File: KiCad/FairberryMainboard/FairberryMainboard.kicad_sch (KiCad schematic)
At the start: 19 parts, among them J1 USB_Header, J2 Conn_02x03_Odd_Even, J3 Conn_02x02_Odd_Even, J4 Conn_01x02, U1 ATmega32U4-MU, U2 BBQ10KBD, Y1 Crystal_GND24

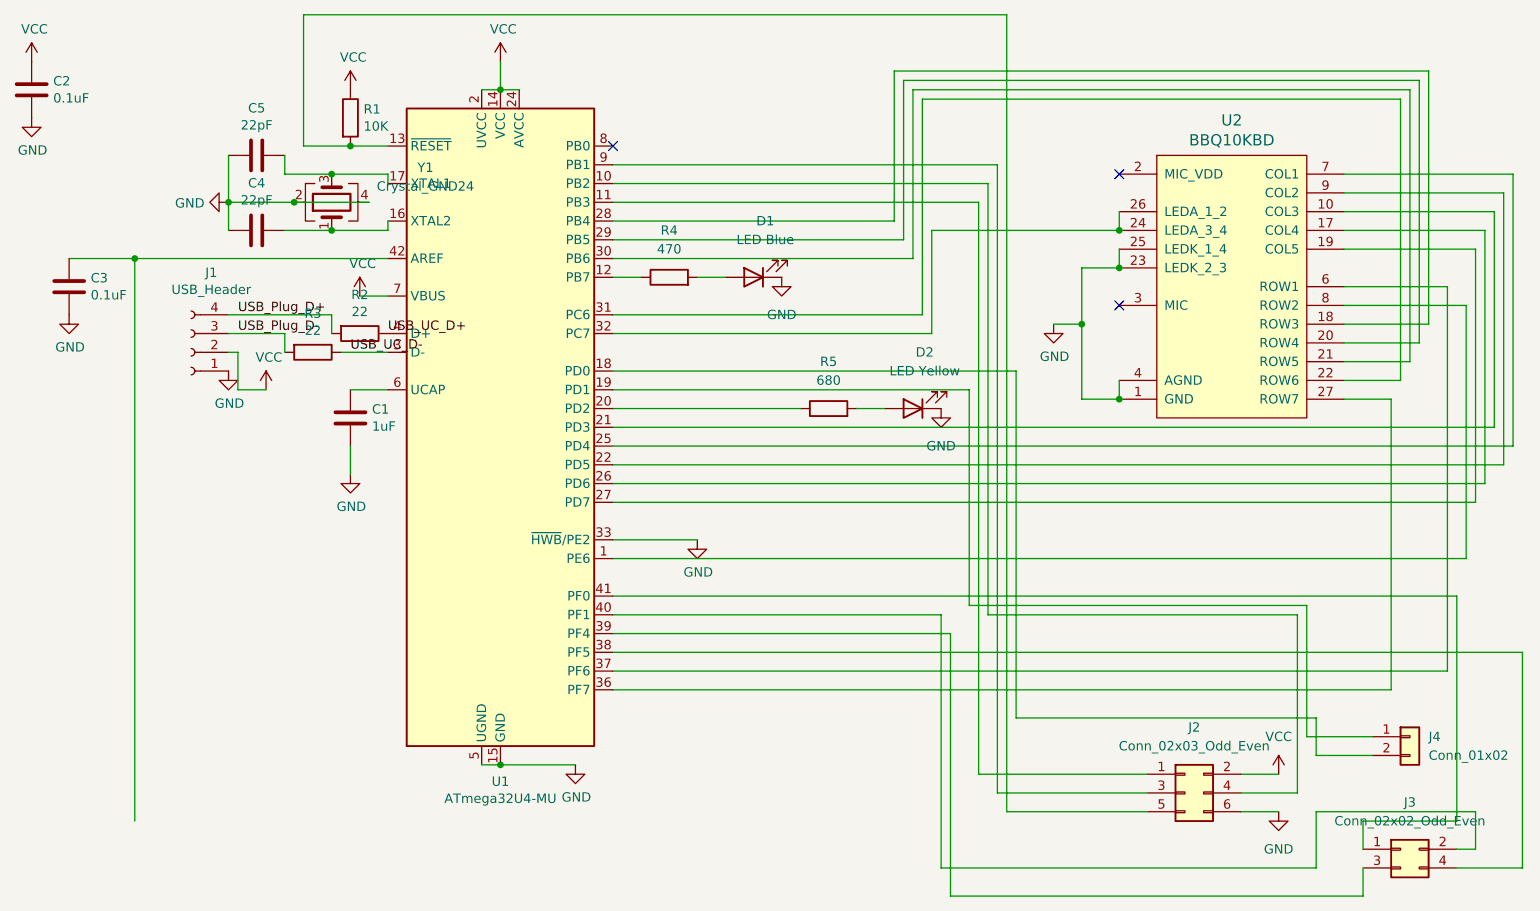
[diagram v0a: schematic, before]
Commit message: Split backlight into two zones, removed status LEDs, reduced y size by 1mm
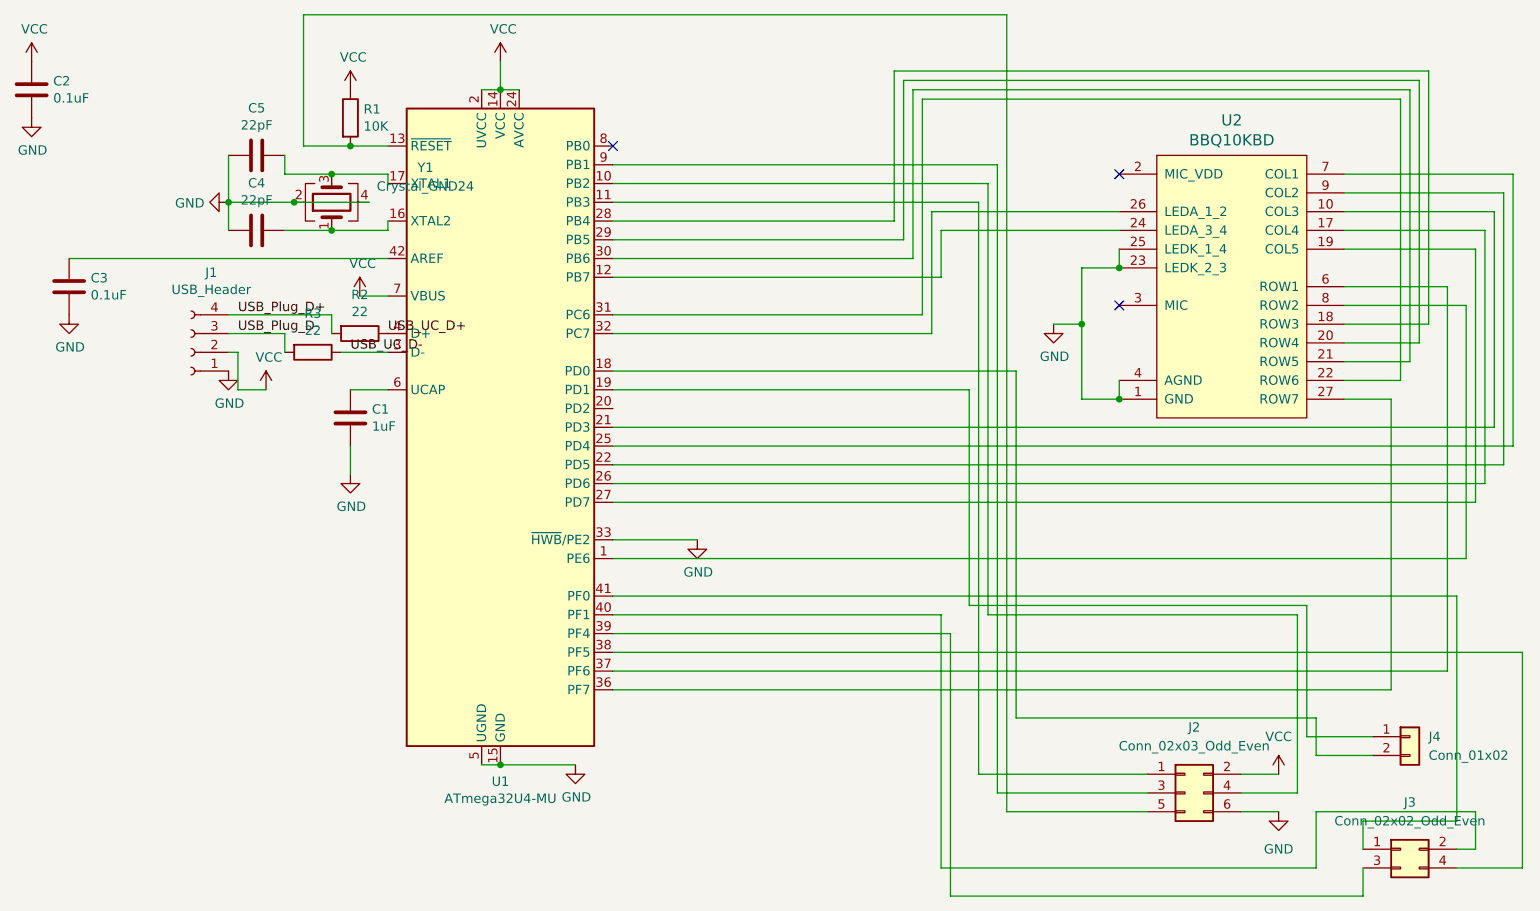
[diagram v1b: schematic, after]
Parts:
- removed D1: LED Blue, LED_SMD:LED_0603_1608Metric, symbol Device:LED
- removed D2: LED Yellow, LED_SMD:LED_0603_1608Metric, symbol Device:LED
- removed R4: 470, Resistor_SMD:R_0402_1005Metric, symbol Device:R
- removed R5: 680, Resistor_SMD:R_0402_1005Metric, symbol Device:R
- J4: footprint Fairberry:TestPoint_Pad_1x2_2.0x3.0mm -> Fairberry:TestPoint_Pad_1x2_2.0x3.0mm_Rotated
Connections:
- net at U1.12 (PB7): now also U2.24 (LEDA_3_4)
- net at U1.32 (PC7), U2.26 (LEDA_1_2): no longer U2.24 (LEDA_3_4)
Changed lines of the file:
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@@
   (junction (at 137.16 140.97) (diameter 0) (color 0 0 0 0)
   )
-  (junction (at 87.63 72.39) (diameter 0) (color 0 0 0 0)
-  )
   (junction (at 109.22 64.77) (diameter 0) (color 0 0 0 0)
   )
   (junction (at 100.33 64.77) (diameter 0) (color 0 0 0 0)
-  )
-  (junction (at 220.98 68.58) (diameter 0) (color 0 0 0 0)
   )
   (junction (at 116.84 57.15) (diameter 0) (color 0 0 0 0)
@@
     (stroke (width 0) (type default) (color 0 0 0 0))
   )
-  (wire (pts (xy 152.4 74.93) (xy 156.21 74.93))
-    (stroke (width 0) (type default) (color 0 0 0 0))
-  )
   (wire (pts (xy 212.09 81.28) (xy 215.9 81.28))
     (stroke (width 0) (type default) (color 0 0 0 0))
   )
-  (wire (pts (xy 195.58 82.55) (xy 195.58 68.58))
+  (wire (pts (xy 195.58 66.04) (xy 195.58 82.55))
     (stroke (width 0) (type default) (color 0 0 0 0))
   )
@@
     (stroke (width 0) (type default) (color 0 0 0 0))
   )
-  (wire (pts (xy 78.74 72.39) (xy 87.63 72.39))
-    (stroke (width 0) (type default) (color 0 0 0 0))
-  )
   (wire (pts (xy 251.46 60.96) (xy 274.32 60.96))
     (stroke (width 0) (type default) (color 0 0 0 0))
@@
     (stroke (width 0) (type default) (color 0 0 0 0))
   )
-  (wire (pts (xy 152.4 92.71) (xy 177.8 92.71))
-    (stroke (width 0) (type default) (color 0 0 0 0))
-  )
   (wire (pts (xy 271.78 66.04) (xy 271.78 95.25))
     (stroke (width 0) (type default) (color 0 0 0 0))
@@
     (stroke (width 0) (type default) (color 0 0 0 0))
   )
-  (wire (pts (xy 185.42 92.71) (xy 189.23 92.71))
-    (stroke (width 0) (type default) (color 0 0 0 0))
-  )
   (wire (pts (xy 193.04 49.53) (xy 193.04 72.39))
     (stroke (width 0) (type default) (color 0 0 0 0))
@@
     (stroke (width 0) (type default) (color 0 0 0 0))
   )
-  (wire (pts (xy 87.63 72.39) (xy 121.92 72.39))
+  (wire (pts (xy 78.74 72.39) (xy 121.92 72.39))
     (stroke (width 0) (type default) (color 0 0 0 0))
   )
@@
     (stroke (width 0) (type default) (color 0 0 0 0))
   )
-  (wire (pts (xy 195.58 68.58) (xy 220.98 68.58))
-    (stroke (width 0) (type default) (color 0 0 0 0))
-  )
   (wire (pts (xy 245.11 144.78) (xy 237.49 144.78))
     (stroke (width 0) (type default) (color 0 0 0 0))
@@
     (stroke (width 0) (type default) (color 0 0 0 0))
   )
-  (wire (pts (xy 87.63 148.59) (xy 87.63 72.39))
-    (stroke (width 0) (type default) (color 0 0 0 0))
-  )
   (wire (pts (xy 191.77 48.26) (xy 191.77 69.85))
     (stroke (width 0) (type default) (color 0 0 0 0))
@@
     (stroke (width 0) (type default) (color 0 0 0 0))
   )
+  (wire (pts (xy 152.4 74.93) (xy 196.85 74.93))
+    (stroke (width 0) (type default) (color 0 0 0 0))
+  )
   (wire (pts (xy 247.65 139.7) (xy 247.65 134.62))
     (stroke (width 0) (type default) (color 0 0 0 0))
@@
     (stroke (width 0) (type default) (color 0 0 0 0))
   )
-  (wire (pts (xy 220.98 66.04) (xy 220.98 68.58))
+  (wire (pts (xy 196.85 68.58) (xy 220.98 68.58))
     (stroke (width 0) (type default) (color 0 0 0 0))
   )
@@
     (stroke (width 0) (type default) (color 0 0 0 0))
   )
-  (wire (pts (xy 163.83 74.93) (xy 167.64 74.93))
-    (stroke (width 0) (type default) (color 0 0 0 0))
-  )
   (wire (pts (xy 107.95 68.58) (xy 114.3 68.58))
     (stroke (width 0) (type default) (color 0 0 0 0))
@@
     (stroke (width 0) (type default) (color 0 0 0 0))
   )
+  (wire (pts (xy 196.85 74.93) (xy 196.85 68.58))
+    (stroke (width 0) (type default) (color 0 0 0 0))
+  )
   (wire (pts (xy 121.92 85.09) (xy 115.57 85.09))
     (stroke (width 0) (type default) (color 0 0 0 0))
@@
   )
   (wire (pts (xy 207.01 87.63) (xy 207.01 134.62))
+    (stroke (width 0) (type default) (color 0 0 0 0))
+  )
+  (wire (pts (xy 195.58 66.04) (xy 220.98 66.04))
     (stroke (width 0) (type default) (color 0 0 0 0))
   )
@@
     (pin "1")
   )
-  (symbol (lib_id "Device:R") (at 160.02 74.93 90) (unit 1)
-    (in_bom yes) (on_board yes) (fields_autoplaced)
-    (property "Reference" "R4" (id 0) (at 160.02 68.58 90))
-    (property "Value" "470" (id 1) (at 160.02 71.12 90))
-    (property "Footprint" "Resistor_SMD:R_0402_1005Metric" (id 2) (at 160.02 76.708 90)
-      (effects (font (size 1.27 1.27)) hide)
-    )
-    (property "Datasheet" "~" (id 3) (at 160.02 74.93 0)
-      (effects (font (size 1.27 1.27)) hide)
-    )
-    (pin "1")
-    (pin "2")
-  )
   (symbol (lib_id "Connector_Generic:Conn_01x02") (at 260.35 137.16 0) (unit 1)
     (in_bom yes) (on_board yes) (fields_autoplaced)
@@
       (effects (font (size 1.27 1.27)) (justify left))
     )
-    (property "Footprint" "Fairberry:TestPoint_Pad_1x2_2.0x3.0mm" (id 2) (at 260.35 137.16 0)
+    (property "Footprint" "Fairberry:TestPoint_Pad_1x2_2.0x3.0mm_Rotated" (id 2) (at 260.35 137.16 0)
       (effects (font (size 1.27 1.27)) hide)
     )
@@
     (pin "1")
     (pin "2")
-  )
-  (symbol (lib_id "power:GND") (at 175.26 74.93 0) (unit 1)
-    (in_bom yes) (on_board yes) (fields_autoplaced)
-    (property "Reference" "#PWR0114" (id 0) (at 175.26 81.28 0)
-      (effects (font (size 1.27 1.27)) hide)
-    )
-    (property "Value" "GND" (id 1) (at 175.26 80.01 0))
-    (property "Footprint" "" (id 2) (at 175.26 74.93 0)
-      (effects (font (size 1.27 1.27)) hide)
-    )
-    (property "Datasheet" "" (id 3) (at 175.26 74.93 0)
-      (effects (font (size 1.27 1.27)) hide)
-    )
-    (pin "1")
   )
   (symbol (lib_id "Device:Crystal_GND24") (at 114.3 64.77 90) (unit 1)
@@
     (pin "4")
   )
-  (symbol (lib_id "Device:LED") (at 171.45 74.93 180) (unit 1)
-    (in_bom yes) (on_board yes) (fields_autoplaced)
-    (property "Reference" "D1" (id 0) (at 173.0375 67.31 0))
-    (property "Value" "LED Blue" (id 1) (at 173.0375 69.85 0))
-    (property "Footprint" "LED_SMD:LED_0603_1608Metric" (id 2) (at 171.45 74.93 0)
-      (effects (font (size 1.27 1.27)) hide)
-    )
-    (property "Datasheet" "https://datasheet.lcsc.com/lcsc/1811101510_Everlight-Elec-19-217-BHC-ZL1M2RY-3T_C72041.pdf" (id 3) (at 171.45 74.93 0)
-      (effects (font (size 1.27 1.27)) hide)
-    )
-    (pin "1")
-    (pin "2")
-  )
   (symbol (lib_id "power:GND") (at 242.57 147.32 0) (unit 1)
     (in_bom yes) (on_board yes) (fields_autoplaced)
@@
     )
     (pin "1")
-  )
-  (symbol (lib_id "Device:LED") (at 193.04 92.71 180) (unit 1)
-    (in_bom yes) (on_board yes) (fields_autoplaced)
-    (property "Reference" "D2" (id 0) (at 194.6275 85.09 0))
-    (property "Value" "LED Yellow" (id 1) (at 194.6275 87.63 0))
-    (property "Footprint" "LED_SMD:LED_0603_1608Metric" (id 2) (at 193.04 92.71 0)
-      (effects (font (size 1.27 1.27)) hide)
-    )
-    (property "Datasheet" "https://datasheet.lcsc.com/lcsc/1810101813_Everlight-Elec-19-213-Y2C-CQ2R2L-3T-CY_C72038.pdf" (id 3) (at 193.04 92.71 0)
-      (effects (font (size 1.27 1.27)) hide)
-    )
-    (pin "1")
-    (pin "2")
   )
   (symbol (lib_id "Connector_Generic:Conn_02x03_Odd_Even") (at 229.87 144.78 0) (unit 1)
@@
     (pin "6")
   )
-  (symbol (lib_id "power:GND") (at 196.85 92.71 0) (unit 1)
-    (in_bom yes) (on_board yes) (fields_autoplaced)
-    (property "Reference" "#PWR0115" (id 0) (at 196.85 99.06 0)
-      (effects (font (size 1.27 1.27)) hide)
-    )
-    (property "Value" "GND" (id 1) (at 196.85 97.79 0))
-    (property "Footprint" "" (id 2) (at 196.85 92.71 0)
-      (effects (font (size 1.27 1.27)) hide)
-    )
-    (property "Datasheet" "" (id 3) (at 196.85 92.71 0)
-      (effects (font (size 1.27 1.27)) hide)
-    )
-    (pin "1")
-  )
-  (symbol (lib_id "Device:R") (at 181.61 92.71 90) (unit 1)
-    (in_bom yes) (on_board yes) (fields_autoplaced)
-    (property "Reference" "R5" (id 0) (at 181.61 86.36 90))
-    (property "Value" "680" (id 1) (at 181.61 88.9 90))
-    (property "Footprint" "Resistor_SMD:R_0402_1005Metric" (id 2) (at 181.61 94.488 90)
-      (effects (font (size 1.27 1.27)) hide)
-    )
-    (property "Datasheet" "~" (id 3) (at 181.61 92.71 0)
-      (effects (font (size 1.27 1.27)) hide)
-    )
-    (pin "1")
-    (pin "2")
-  )
   (symbol (lib_id "power:VCC") (at 242.57 142.24 0) (unit 1)
     (in_bom yes) (on_board yes) (fields_autoplaced)
@@
       (reference "#PWR0113") (unit 1) (value "GND") (footprint "")
     )
-    (path "/31836a5c-a49e-488d-99c5-485932504811"
-      (reference "#PWR0114") (unit 1) (value "GND") (footprint "")
-    )
-    (path "/ce37f8b2-536a-4acd-a58b-79008d61cc8a"
-      (reference "#PWR0115") (unit 1) (value "GND") (footprint "")
-    )
     (path "/f0fb6453-26be-4fd7-aae7-261ab6376c65"
       (reference "#PWR0116") (unit 1) (value "VCC") (footprint "")
@@
       (reference "C5") (unit 1) (value "22pF") (footprint "Capacitor_SMD:C_0402_1005Metric")
     )
-    (path "/86b91b71-a5d2-432e-bd76-a62af5b970ae"
-      (reference "D1") (unit 1) (value "LED Blue") (footprint "LED_SMD:LED_0603_1608Metric")
-    )
-    (path "/b623db80-f671-4b08-b8dc-53e54df71675"
-      (reference "D2") (unit 1) (value "LED Yellow") (footprint "LED_SMD:LED_0603_1608Metric")
-    )
     (path "/00000000-0000-0000-0000-00006286c9e0"
       (reference "J1") (unit 1) (value "USB_Header") (footprint "Fairberry:TestPoint_Pad_2x2_2.0x3.0mm")
@@
     )
     (path "/05157f33-dcd2-4789-b6b5-f7fba29ec790"
-      (reference "J4") (unit 1) (value "Conn_01x02") (footprint "Fairberry:TestPoint_Pad_1x2_2.0x3.0mm")
+      (reference "J4") (unit 1) (value "Conn_01x02") (footprint "Fairberry:TestPoint_Pad_1x2_2.0x3.0mm_Rotated")
     )
     (path "/00000000-0000-0000-0000-000062855b81"
@@
       (reference "R3") (unit 1) (value "22") (footprint "Resistor_SMD:R_0603_1608Metric")
     )
-    (path "/033b710a-2211-470a-9bc8-fbc5d5025404"
-      (reference "R4") (unit 1) (value "470") (footprint "Resistor_SMD:R_0402_1005Metric")
-    )
-    (path "/da4cac2e-5558-4956-b688-63640fc9edbc"
-      (reference "R5") (unit 1) (value "680") (footprint "Resistor_SMD:R_0402_1005Metric")
-    )
     (path "/00000000-0000-0000-0000-00006283f827"

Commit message: Finished v0.3.0
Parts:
- J3: footprint Fairberry:TestPoint_Pad_1+3_2.0x3.0mm_slim -> Fairberry:TestPoint_Pad_2+2_Z_2.0x2.0mm
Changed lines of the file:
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@@
     (property "Reference" "J3" (id 0) (at 260.35 146.05 0))
     (property "Value" "Conn_02x02_Odd_Even" (id 1) (at 260.35 148.59 0))
-    (property "Footprint" "Fairberry:TestPoint_Pad_1+3_2.0x3.0mm_slim" (id 2) (at 259.08 152.4 0)
+    (property "Footprint" "Fairberry:TestPoint_Pad_2+2_Z_2.0x2.0mm" (id 2) (at 259.08 152.4 0)
       (effects (font (size 1.27 1.27)) hide)
     )
@@
     )
     (path "/71012496-527d-4cd0-a6dc-811c461127a0"
-      (reference "J3") (unit 1) (value "Conn_02x02_Odd_Even") (footprint "Fairberry:TestPoint_Pad_1+3_2.0x3.0mm_slim")
+      (reference "J3") (unit 1) (value "Conn_02x02_Odd_Even") (footprint "Fairberry:TestPoint_Pad_2+2_Z_2.0x2.0mm")
     )
     (path "/05157f33-dcd2-4789-b6b5-f7fba29ec790"
